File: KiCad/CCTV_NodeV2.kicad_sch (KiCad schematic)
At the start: 9 parts, among them J1 Solar 6V/10W, J2 Battery (ext, 2× 18650 ||), U1 CN3791, U2 TC4056A_BMS, U3 MT3608, U4 ESP32-S3-DevKitC-1 N16R8, U5 OV7670

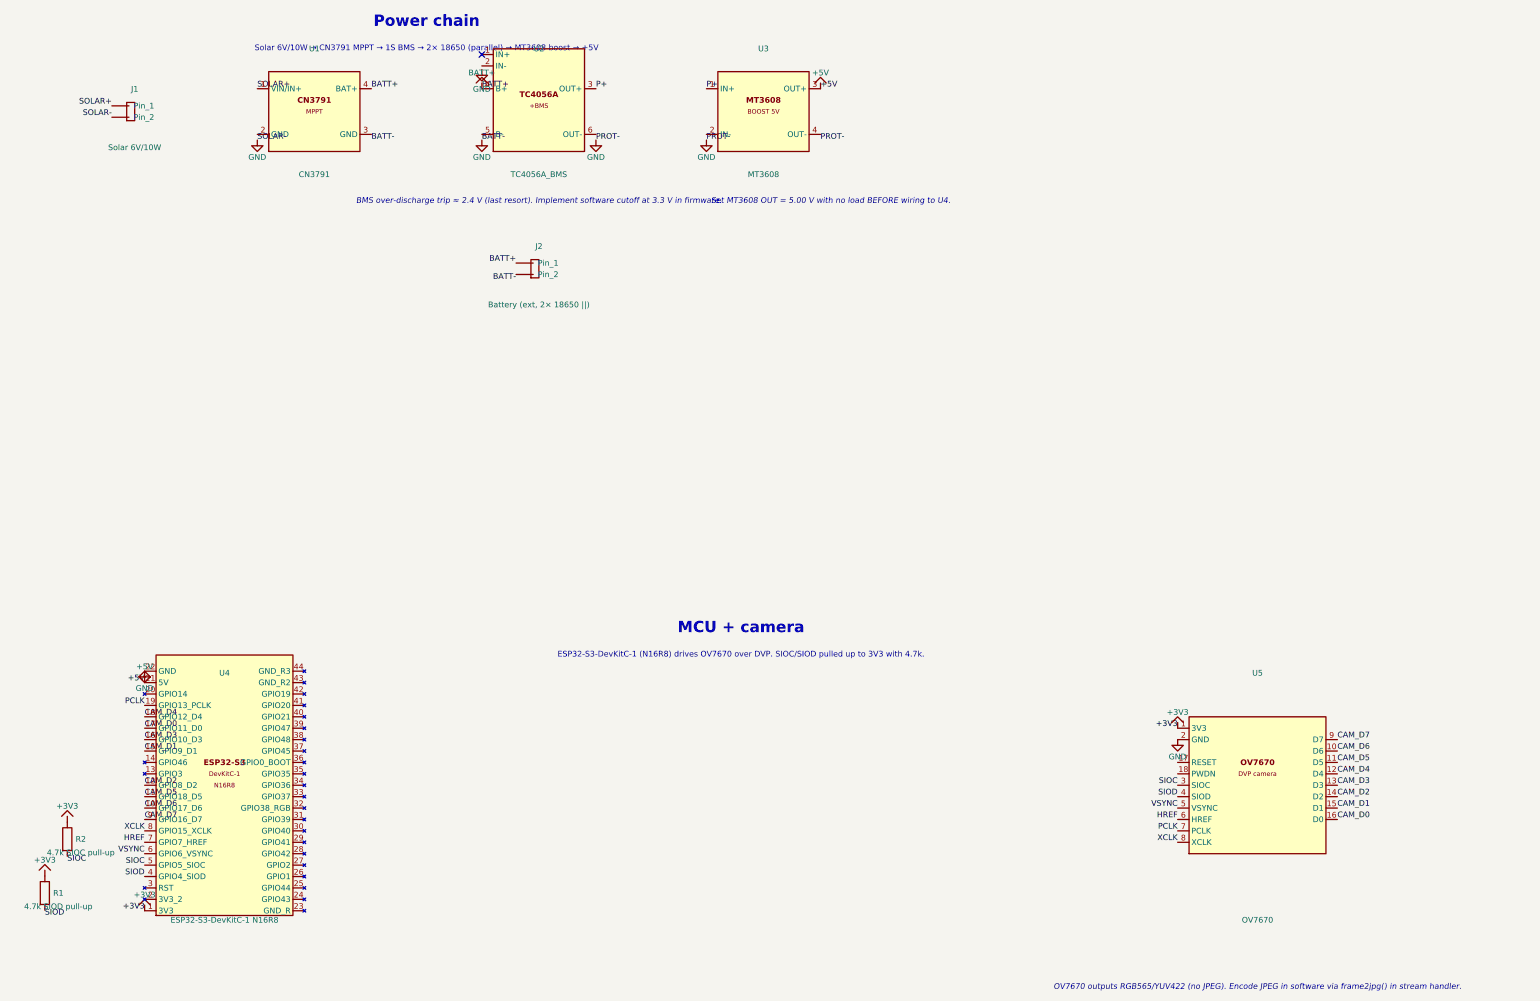
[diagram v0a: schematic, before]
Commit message: Save manually adjusted schematic and footprints
KiCad/CCTV_NodeV2.kicad_sch:
- Manual layout adjustments in eeschema (component positions,
  label positions, wire routing, annotations)

KiCad/CCTV_NodeV2.kicad_pro:
- Project settings updated by KiCad (DRC rules, pad defaults)

KiCad/CCTV_RPi4.pretty/CN3791_Module.kicad_mod:
- Footprint geometry updated by KiCad editor

KiCad/CCTV_RPi4.pretty/MT3608_Module.kicad_mod:
- Footprint geometry updated by KiCad editor
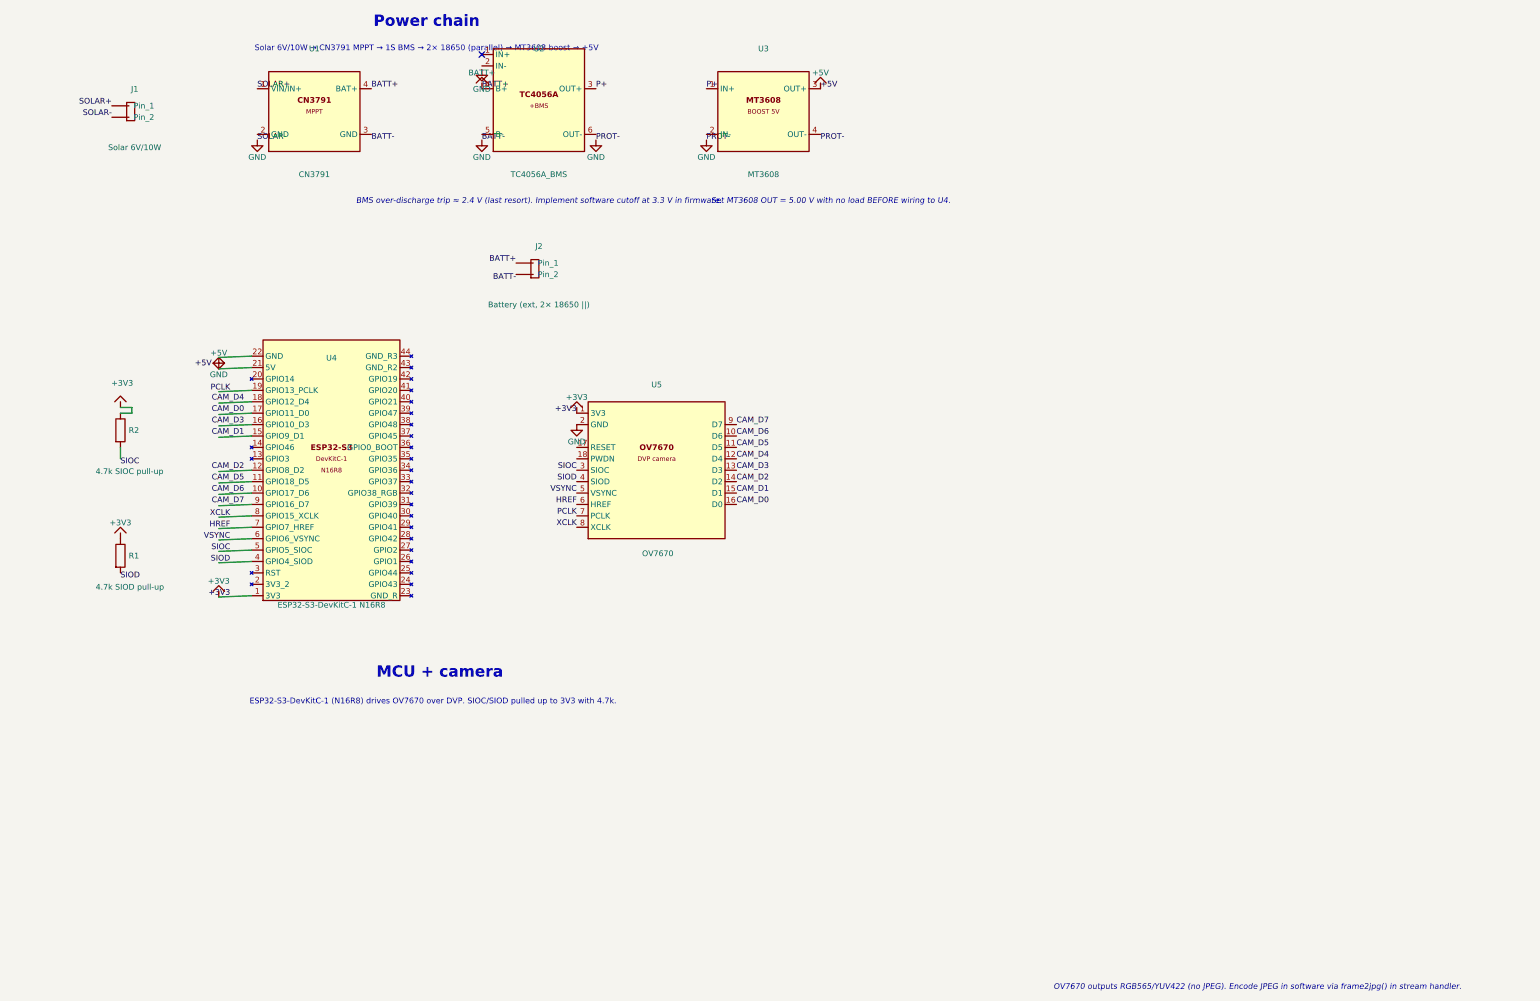
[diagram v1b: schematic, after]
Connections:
- net CAM_D0: no longer U4.17 (GPIO11_D0)
- net CAM_D1: no longer U4.15 (GPIO9_D1)
- net CAM_D2: no longer U4.12 (GPIO8_D2)
- net CAM_D3: no longer U4.16 (GPIO10_D3)
- net CAM_D4: no longer U4.18 (GPIO12_D4)
- net CAM_D5: no longer U4.11 (GPIO18_D5)
- net CAM_D6: no longer U4.10 (GPIO17_D6)
- net CAM_D7: no longer U4.9 (GPIO16_D7)
- net HREF: no longer U4.7 (GPIO7_HREF)
- net PCLK: no longer U4.19 (GPIO13_PCLK)
- net SIOC: no longer U4.5 (GPIO5_SIOC)
- net SIOD: no longer U4.4 (GPIO4_SIOD)
- net VSYNC: no longer U4.6 (GPIO6_VSYNC)
- net XCLK: no longer U4.8 (GPIO15_XCLK)
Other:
- moved on the sheet: R1, R2, U4, U5

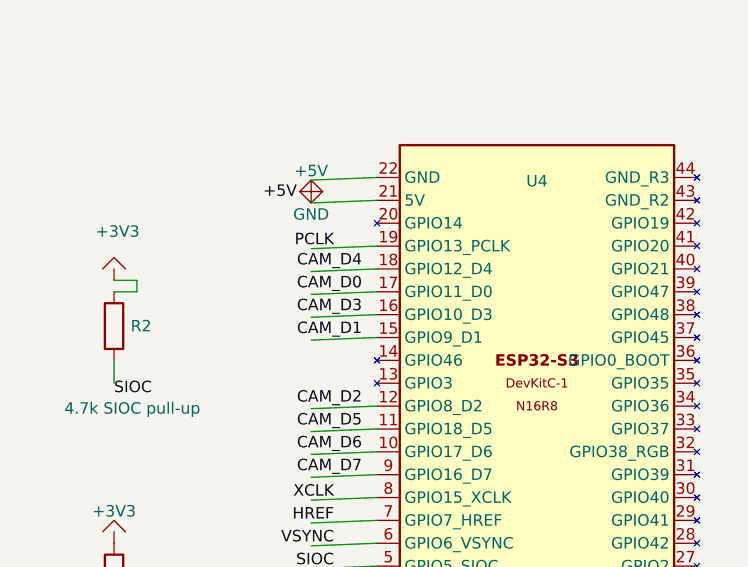
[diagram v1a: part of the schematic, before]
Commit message: Fix unconnected U4 pin 17 (CAM_D0) — move label to wire endpoint
The CAM_D0 label near U4 was at (57.15, 137.16) but the wire
from U4 pin 17 ends at (58.73, 137.45) — a small gap causing
ERC 'pin unconnected' error.

Connection chain after fix:
  U4 pin 17 (GPIO11_D0) at (66.04, 137.16)
    → wire → (58.73, 137.45)
    ← label 'CAM_D0'  ← (moved from 57.15,137.16)
    → connects by name to →
  U5 pin 16 (D0) label 'CAM_D0' at (173.99, 157.48) ✓
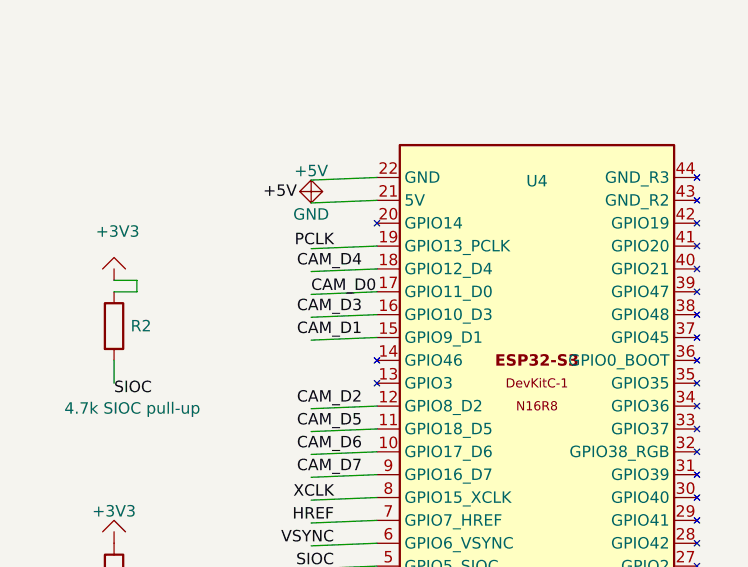
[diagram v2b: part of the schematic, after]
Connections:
- net CAM_D0: now also U4.17 (GPIO11_D0)
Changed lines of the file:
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@@
 	)
 	(label "CAM_D0"
-		(at 57.15 137.16 0)
+		(at 58.73 137.45 0)
 		(effects
 			(font

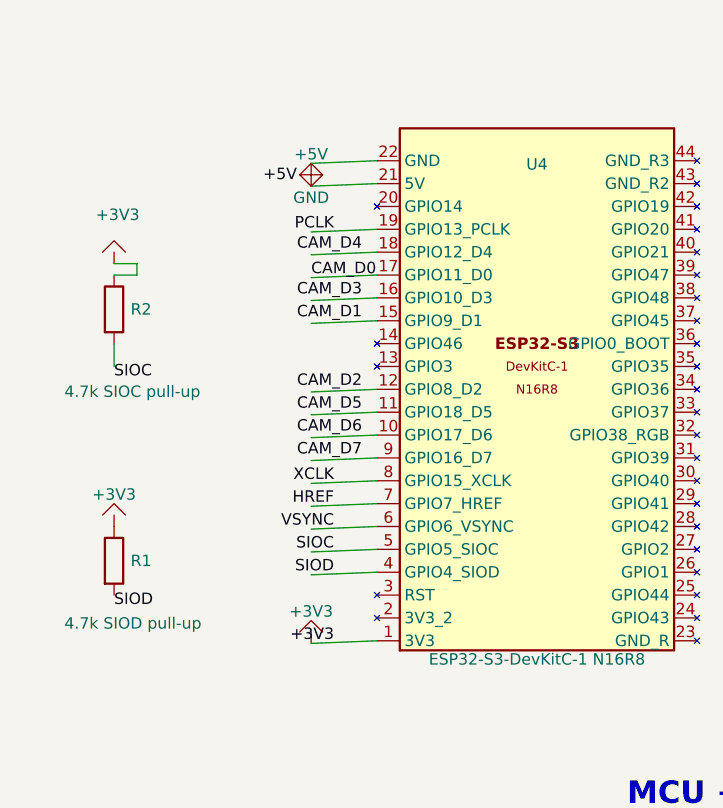
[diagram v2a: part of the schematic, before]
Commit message: Fix all U4 label gaps — move labels to wire endpoints
All U4 pin wires run from pin endpoint (66.04, y_pin) to
(58.73, y_pin+0.29). Labels were at either x=57.15 (wrong x
and wrong y) or x=61.27 (wrong x, correct y), causing
'pin unconnected' ERC errors on every U4 signal pin.

Fixed 15 positions by moving all labels to (58.73, y_wire_end):

x=57.15 labels (CAM signals + power):
  CAM_D7 : (57.15,157.48) → (58.73,157.77)
  CAM_D6 : (57.15,154.94) → (58.73,155.23)
  CAM_D5 : (57.15,152.40) → (58.73,152.69)
  CAM_D2 : (57.15,149.86) → (58.73,150.15)
  CAM_D1 : (57.15,142.24) → (58.73,142.53)
  CAM_D3 : (57.15,139.70) → (58.73,139.99)
  CAM_D4 : (57.15,134.62) → (58.73,134.91)
  +5V    : (57.15,127.00) → (58.73,127.29)

x=61.27 labels (control signals + 3V3):
  +3V3   : (61.27,178.09) → (58.73,178.09)
  SIOD   : (61.27,170.47) → (58.73,170.47)
  SIOC   : (61.27,167.93) → (58.73,167.93)
  VSYNC  : (61.27,165.39) → (58.73,165.39)
  HREF   : (61.27,162.85) → (58.73,162.85)
  XCLK   : (61.27,160.31) → (58.73,160.31)
  PCLK   : (61.27,132.37) → (58.73,132.37)

Also fixed angle=180 property variants and y values
without trailing zeros (127, 139.7, 152.4).

U5 labels (x=138.43 left, x=173.99 right) were already
at correct pin endpoints — no changes needed.
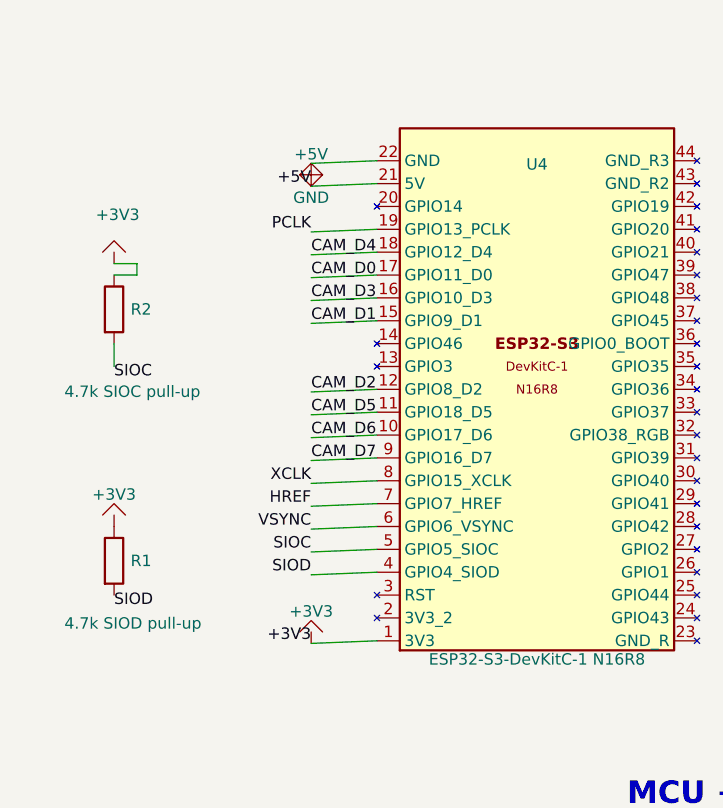
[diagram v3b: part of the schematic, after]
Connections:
- net CAM_D1: now also U4.15 (GPIO9_D1)
- net CAM_D2: now also U4.12 (GPIO8_D2)
- net CAM_D3: now also U4.16 (GPIO10_D3)
- net CAM_D4: now also U4.18 (GPIO12_D4)
- net CAM_D5: now also U4.11 (GPIO18_D5)
- net CAM_D6: now also U4.10 (GPIO17_D6)
- net CAM_D7: now also U4.9 (GPIO16_D7)
- net HREF: now also U4.7 (GPIO7_HREF)
- net PCLK: now also U4.19 (GPIO13_PCLK)
- net SIOC: now also U4.5 (GPIO5_SIOC)
- net SIOD: now also U4.4 (GPIO4_SIOD)
- net VSYNC: now also U4.6 (GPIO6_VSYNC)
- net XCLK: now also U4.8 (GPIO15_XCLK)
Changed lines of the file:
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@@
 	)
 	(label "+5V"
-		(at 57.15 127 180)
+		(at 58.73 127.29 180)
 		(effects
 			(font
@@
 	)
 	(label "+3V3"
-		(at 61.27 178.09 180)
+		(at 58.73 178.09 180)
 		(effects
 			(font
@@
 	)
 	(label "SIOD"
-		(at 61.27 170.47 180)
+		(at 58.73 170.47 180)
 		(effects
 			(font
@@
 	)
 	(label "SIOC"
-		(at 61.27 167.93 180)
+		(at 58.73 167.93 180)
 		(effects
 			(font
@@
 	)
 	(label "VSYNC"
-		(at 61.27 165.39 180)
+		(at 58.73 165.39 180)
 		(effects
 			(font
@@
 	)
 	(label "HREF"
-		(at 61.27 162.85 180)
+		(at 58.73 162.85 180)
 		(effects
 			(font
@@
 	)
 	(label "PCLK"
-		(at 61.27 132.37 180)
+		(at 58.73 132.37 180)
 		(effects
 			(font
@@
 	)
 	(label "XCLK"
-		(at 61.27 160.31 180)
+		(at 58.73 160.31 180)
 		(effects
 			(font
@@
 	)
 	(label "CAM_D1"
-		(at 57.15 142.24 0)
+		(at 58.73 142.53 0)
 		(effects
 			(font
@@
 	)
 	(label "CAM_D2"
-		(at 57.15 149.86 0)
+		(at 58.73 150.15 0)
 		(effects
 			(font
@@
 	)
 	(label "CAM_D3"
-		(at 57.15 139.7 0)
+		(at 58.73 139.99 0)
 		(effects
 			(font
@@
 	)
 	(label "CAM_D4"
-		(at 57.15 134.62 0)
+		(at 58.73 134.91 0)
 		(effects
 			(font
@@
 	)
 	(label "CAM_D5"
-		(at 57.15 152.4 0)
+		(at 58.73 152.69 0)
 		(effects
 			(font
@@
 	)
 	(label "CAM_D6"
-		(at 57.15 154.94 0)
+		(at 58.73 155.23 0)
 		(effects
 			(font
@@
 	)
 	(label "CAM_D7"
-		(at 57.15 157.48 0)
+		(at 58.73 157.77 0)
 		(effects
 			(font

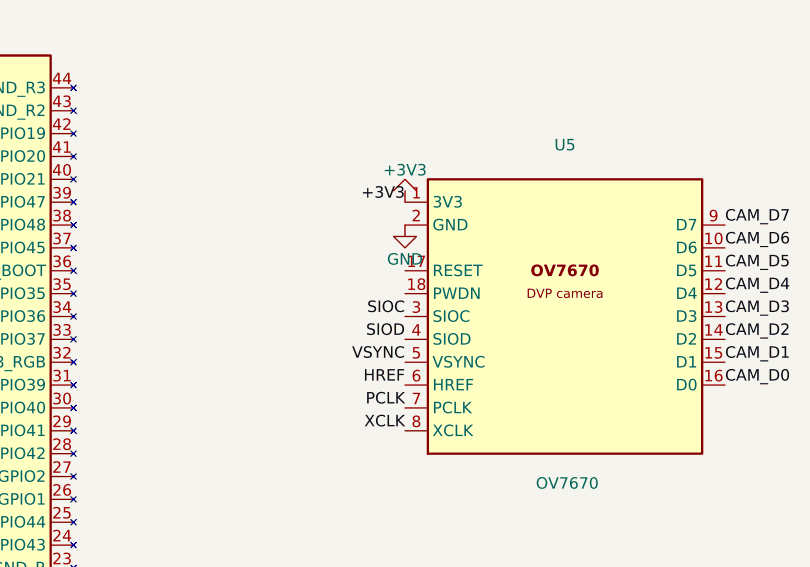
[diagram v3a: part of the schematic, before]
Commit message: Connect U5 OV7670 pin17 RESET to +3V3 and pin18 PWDN to GND
Pins 17 (RESET) and 18 (PWDN) were unconnected, which causes the
OV7670 sensor to behave unpredictably:
  - RESET floating → spurious resets or sensor stuck in reset
  - PWDN floating → sensor may enter power-down randomly

Correct connections for normal operation:
  Pin 17 RESET (138.43, 144.78) → +3V3 (active-low reset, HIGH = run)
  Pin 18 PWDN  (138.43, 147.32) → GND  (active-high power-down, LOW = run)

Added two power symbols at the pin endpoints.
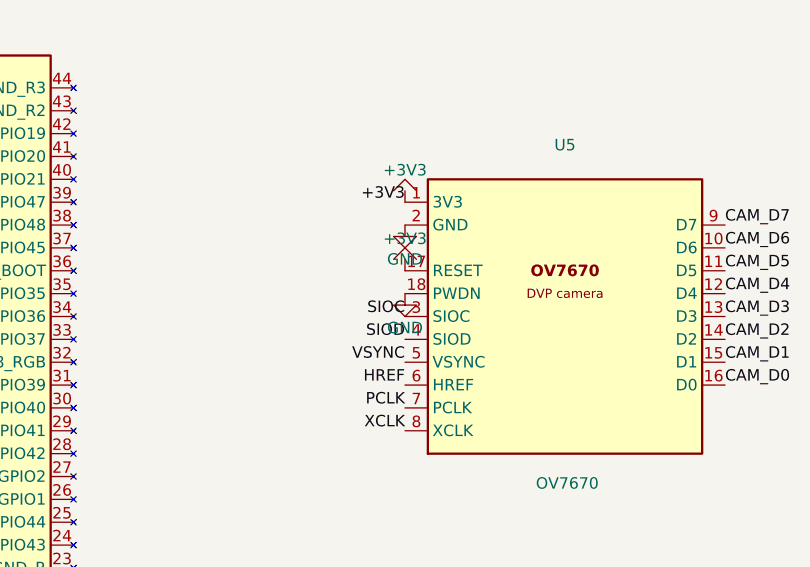
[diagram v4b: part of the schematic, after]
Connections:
- net +3V3: now also U5.17 (RESET)
- net GND: now also U5.18 (PWDN)
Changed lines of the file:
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@@
+		)
+	)
+	(symbol
+		(lib_id "CCTV2:+3V3")
+		(at 138.43 144.78 0)
+		(unit 1)
+		(body_style 1)
+		(exclude_from_sim no)
+		(in_bom yes)
+		(on_board yes)
+		(in_pos_files yes)
+		(dnp no)
+		(property "Reference" "#PWR_RESET"
+			(at 138.43 140.97 0)
+			(hide yes)
+			(show_name no)
+			(do_not_autoplace no)
+			(effects (font (size 1.27 1.27)))
+		)
+		(property "Value" "+3V3"
+			(at 138.43 141.22 0)
+			(show_name no)
+			(do_not_autoplace no)
+			(effects (font (size 1.27 1.27)))
+		)
+		(pin "1")
+		(instances
+			(project "CCTV_NodeV2"
+				(path "/b0c0d0e0-0001-4000-8000-000000000001"
+					(reference "#PWR_RESET")
+					(unit 1)
+				)
+			)
+		)
+	)
+	(symbol
+		(lib_id "CCTV2:GND")
+		(at 138.43 147.32 0)
+		(unit 1)
+		(body_style 1)
+		(exclude_from_sim no)
+		(in_bom yes)
+		(on_board yes)
+		(in_pos_files yes)
+		(dnp no)
+		(property "Reference" "#PWR_PWDN"
+			(at 138.43 153.67 0)
+			(hide yes)
+			(show_name no)
+			(do_not_autoplace no)
+			(effects (font (size 1.27 1.27)))
+		)
+		(property "Value" "GND"
+			(at 138.43 151.13 0)
+			(show_name no)
+			(do_not_autoplace no)
+			(effects (font (size 1.27 1.27)))
+		)
+		(pin "1")
+		(instances
+			(project "CCTV_NodeV2"
+				(path "/b0c0d0e0-0001-4000-8000-000000000001"
+					(reference "#PWR_PWDN")
+					(unit 1)
+				)
+			)
 		)
 	)
